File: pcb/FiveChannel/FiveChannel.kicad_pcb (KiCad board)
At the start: 2 copper layers, 47 x 31.4 mm, 22 parts, among them J101 UPDI, J102 5V In, J103 Conn_01x04_Male, J104 Conn_01x07_Male, J201 Conn_01x20_Male, U101 74LS595, U102 ATTINY1614

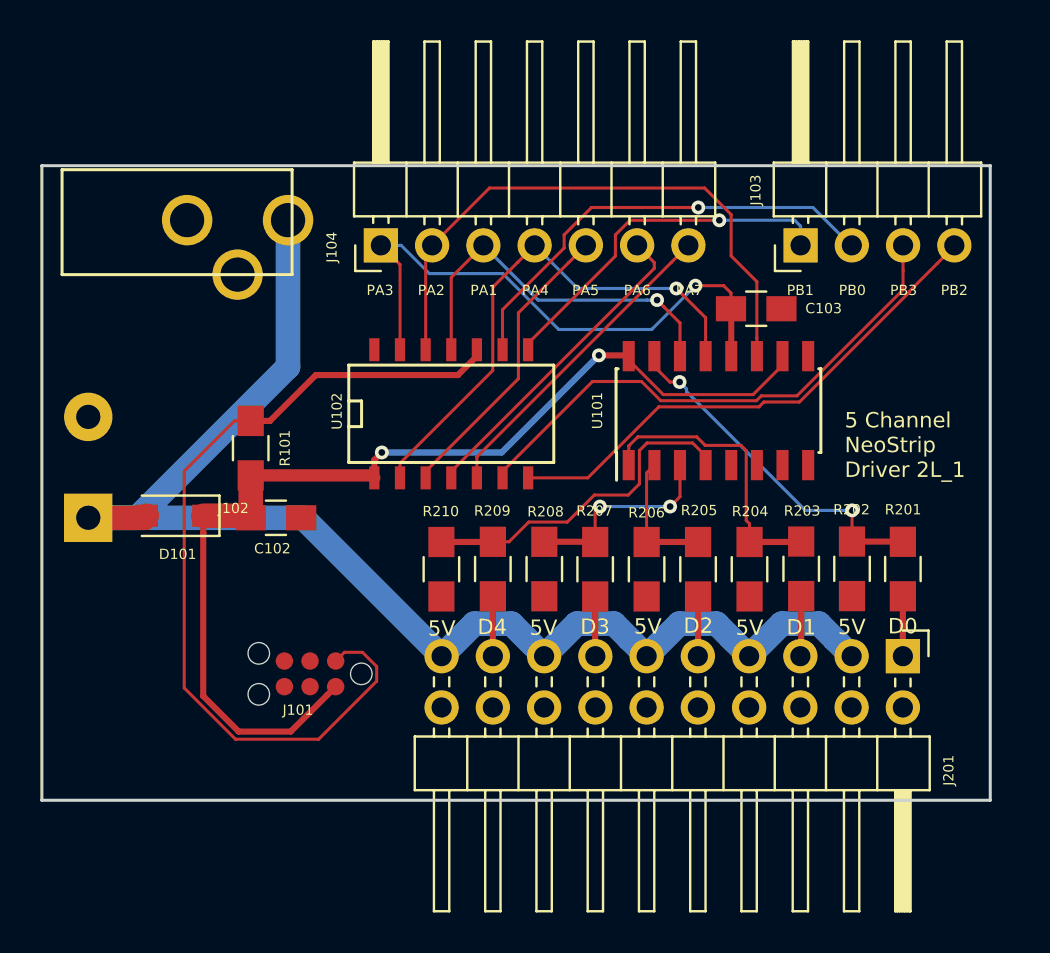
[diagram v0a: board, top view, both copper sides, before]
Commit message: Updates the schematic and PCB design to the lastest from the original repo
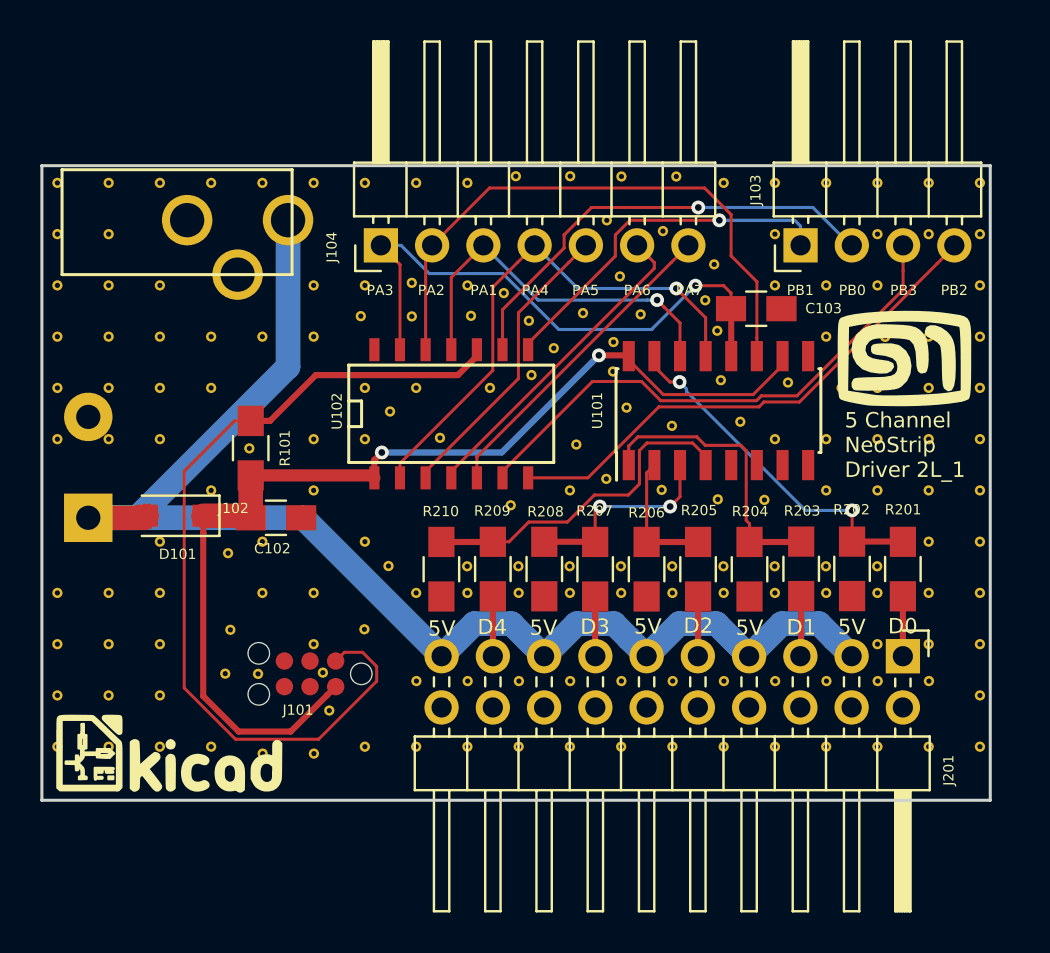
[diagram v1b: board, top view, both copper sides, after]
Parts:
- added G***: LOGO, advent_sternla:KiCad-Logo, F.Cu at (133.0, 78.5)
- added G***: LOGO, advent_sternla:MyBasic_rounded_50_1, F.Cu at (169.4, 58.9)
- added G***: LOGO, advent_sternla:MyBasic_rounded_50_1, B.Cu at (157.0, 64.3)
- added REF***: KiCad-Logo2_6mm_SilkScreen, Symbols:KiCad-Logo2_6mm_SilkScreen, B.Cu at (169.6, 64.2)
- added ST**: STITCH_VIA, advent_sternla:STITCH_VIA, F.Cu at (127.4, 50.3)
- added ST**: STITCH_VIA, advent_sternla:STITCH_VIA, F.Cu at (150.1, 49.9)
- added ST**: STITCH_VIA, advent_sternla:STITCH_VIA, F.Cu at (165.5, 65.5)
- added ST**: STITCH_VIA, advent_sternla:STITCH_VIA, F.Cu at (168.1, 65.5)
- added ST**: STITCH_VIA, advent_sternla:STITCH_VIA, F.Cu at (170.6, 65.5)
- added ST**: STITCH_VIA, advent_sternla:STITCH_VIA, F.Cu at (173.1, 65.5)
- added ST**: STITCH_VIA, advent_sternla:STITCH_VIA, F.Cu at (132.5, 68.0)
- added ST**: STITCH_VIA, advent_sternla:STITCH_VIA, F.Cu at (135.9, 68.6)
- added ST**: STITCH_VIA, advent_sternla:STITCH_VIA, F.Cu at (137.6, 68.0)
- added ST**: STITCH_VIA, advent_sternla:STITCH_VIA, F.Cu at (142.7, 68.0)
- added ST**: STITCH_VIA, advent_sternla:STITCH_VIA, F.Cu at (143.8, 69.2)
- added ST**: STITCH_VIA, advent_sternla:STITCH_VIA, F.Cu at (147.7, 69.3)
- added ST**: STITCH_VIA, advent_sternla:STITCH_VIA, F.Cu at (152.8, 49.9)
- added ST**: STITCH_VIA, advent_sternla:STITCH_VIA, F.Cu at (150.3, 69.3)
- added ST**: STITCH_VIA, advent_sternla:STITCH_VIA, F.Cu at (152.8, 69.3)
- added ST**: STITCH_VIA, advent_sternla:STITCH_VIA, F.Cu at (155.3, 69.3)
- added ST**: STITCH_VIA, advent_sternla:STITCH_VIA, F.Cu at (157.9, 69.3)
- added ST**: STITCH_VIA, advent_sternla:STITCH_VIA, F.Cu at (160.4, 69.3)
- added ST**: STITCH_VIA, advent_sternla:STITCH_VIA, F.Cu at (163.0, 69.3)
- added ST**: STITCH_VIA, advent_sternla:STITCH_VIA, F.Cu at (165.5, 69.3)
- added ST**: STITCH_VIA, advent_sternla:STITCH_VIA, F.Cu at (168.0, 69.3)
- added ST**: STITCH_VIA, advent_sternla:STITCH_VIA, F.Cu at (170.6, 68.0)
- added ST**: STITCH_VIA, advent_sternla:STITCH_VIA, F.Cu at (173.1, 68.0)
- added ST**: STITCH_VIA, advent_sternla:STITCH_VIA, F.Cu at (155.4, 49.9)
- added ST**: STITCH_VIA, advent_sternla:STITCH_VIA, F.Cu at (127.4, 70.6)
- added ST**: STITCH_VIA, advent_sternla:STITCH_VIA, F.Cu at (130.0, 70.6)
- added ST**: STITCH_VIA, advent_sternla:STITCH_VIA, F.Cu at (132.5, 70.6)
- added ST**: STITCH_VIA, advent_sternla:STITCH_VIA, F.Cu at (137.6, 70.6)
- added ST**: STITCH_VIA, advent_sternla:STITCH_VIA, F.Cu at (140.1, 70.6)
- added ST**: STITCH_VIA, advent_sternla:STITCH_VIA, F.Cu at (145.2, 70.6)
- added ST**: STITCH_VIA, advent_sternla:STITCH_VIA, F.Cu at (147.7, 70.6)
- added ST**: STITCH_VIA, advent_sternla:STITCH_VIA, F.Cu at (150.3, 70.6)
- added ST**: STITCH_VIA, advent_sternla:STITCH_VIA, F.Cu at (152.8, 70.6)
- added ST**: STITCH_VIA, advent_sternla:STITCH_VIA, F.Cu at (155.4, 70.6)
- added ST**: STITCH_VIA, advent_sternla:STITCH_VIA, F.Cu at (158.1, 49.9)
- added ST**: STITCH_VIA, advent_sternla:STITCH_VIA, F.Cu at (157.9, 70.6)
- added ST**: STITCH_VIA, advent_sternla:STITCH_VIA, F.Cu at (160.4, 70.6)
- added ST**: STITCH_VIA, advent_sternla:STITCH_VIA, F.Cu at (163.0, 70.6)
- added ST**: STITCH_VIA, advent_sternla:STITCH_VIA, F.Cu at (165.5, 70.6)
- added ST**: STITCH_VIA, advent_sternla:STITCH_VIA, F.Cu at (168.1, 70.6)
- added ST**: STITCH_VIA, advent_sternla:STITCH_VIA, F.Cu at (170.6, 70.6)
- added ST**: STITCH_VIA, advent_sternla:STITCH_VIA, F.Cu at (173.1, 70.6)
- added ST**: STITCH_VIA, advent_sternla:STITCH_VIA, F.Cu at (127.4, 73.1)
- added ST**: STITCH_VIA, advent_sternla:STITCH_VIA, F.Cu at (130.0, 73.1)
- added ST**: STITCH_VIA, advent_sternla:STITCH_VIA, F.Cu at (132.5, 73.1)
- added ST**: STITCH_VIA, advent_sternla:STITCH_VIA, F.Cu at (160.4, 50.3)
- added ST**: STITCH_VIA, advent_sternla:STITCH_VIA, F.Cu at (137.4, 74.6)
- added ST**: STITCH_VIA, advent_sternla:STITCH_VIA, F.Cu at (140.1, 73.1)
- added ST**: STITCH_VIA, advent_sternla:STITCH_VIA, F.Cu at (142.6, 72.4)
- added ST**: STITCH_VIA, advent_sternla:STITCH_VIA, F.Cu at (168.1, 73.1)
- added ST**: STITCH_VIA, advent_sternla:STITCH_VIA, F.Cu at (170.6, 73.1)
- added ST**: STITCH_VIA, advent_sternla:STITCH_VIA, F.Cu at (173.1, 73.1)
- added ST**: STITCH_VIA, advent_sternla:STITCH_VIA, F.Cu at (127.4, 75.7)
- added ST**: STITCH_VIA, advent_sternla:STITCH_VIA, F.Cu at (130.0, 75.7)
- added ST**: STITCH_VIA, advent_sternla:STITCH_VIA, F.Cu at (132.5, 75.7)
- added ST**: STITCH_VIA, advent_sternla:STITCH_VIA, F.Cu at (136.0, 72.4)
- added ST**: STITCH_VIA, advent_sternla:STITCH_VIA, F.Cu at (163.0, 50.3)
- added ST**: STITCH_VIA, advent_sternla:STITCH_VIA, F.Cu at (140.6, 74.5)
- added ST**: STITCH_VIA, advent_sternla:STITCH_VIA, F.Cu at (140.9, 76.4)
- added ST**: STITCH_VIA, advent_sternla:STITCH_VIA, F.Cu at (145.2, 74.9)
- added ST**: STITCH_VIA, advent_sternla:STITCH_VIA, F.Cu at (147.8, 74.9)
- added ST**: STITCH_VIA, advent_sternla:STITCH_VIA, F.Cu at (150.3, 74.9)
- added ST**: STITCH_VIA, advent_sternla:STITCH_VIA, F.Cu at (152.8, 74.9)
- added ST**: STITCH_VIA, advent_sternla:STITCH_VIA, F.Cu at (155.4, 74.9)
- added ST**: STITCH_VIA, advent_sternla:STITCH_VIA, F.Cu at (157.9, 74.9)
- added ST**: STITCH_VIA, advent_sternla:STITCH_VIA, F.Cu at (160.5, 74.9)
- added ST**: STITCH_VIA, advent_sternla:STITCH_VIA, F.Cu at (163.0, 74.9)
- added ST**: STITCH_VIA, advent_sternla:STITCH_VIA, F.Cu at (165.5, 50.3)
- added ST**: STITCH_VIA, advent_sternla:STITCH_VIA, F.Cu at (165.5, 74.9)
- added ST**: STITCH_VIA, advent_sternla:STITCH_VIA, F.Cu at (168.1, 74.9)
- added ST**: STITCH_VIA, advent_sternla:STITCH_VIA, F.Cu at (170.6, 74.9)
- added ST**: STITCH_VIA, advent_sternla:STITCH_VIA, F.Cu at (173.1, 75.7)
- added ST**: STITCH_VIA, advent_sternla:STITCH_VIA, F.Cu at (127.4, 78.2)
- added ST**: STITCH_VIA, advent_sternla:STITCH_VIA, F.Cu at (130.0, 78.2)
- added ST**: STITCH_VIA, advent_sternla:STITCH_VIA, F.Cu at (132.5, 78.2)
- added ST**: STITCH_VIA, advent_sternla:STITCH_VIA, F.Cu at (135.0, 78.2)
- added ST**: STITCH_VIA, advent_sternla:STITCH_VIA, F.Cu at (137.6, 78.5)
- added ST**: STITCH_VIA, advent_sternla:STITCH_VIA, F.Cu at (140.1, 78.5)
- added ST**: STITCH_VIA, advent_sternla:STITCH_VIA, F.Cu at (168.1, 50.3)
- added ST**: STITCH_VIA, advent_sternla:STITCH_VIA, F.Cu at (142.7, 78.2)
- added ST**: STITCH_VIA, advent_sternla:STITCH_VIA, F.Cu at (145.2, 78.2)
- added ST**: STITCH_VIA, advent_sternla:STITCH_VIA, F.Cu at (147.7, 78.2)
- added ST**: STITCH_VIA, advent_sternla:STITCH_VIA, F.Cu at (150.3, 78.2)
- added ST**: STITCH_VIA, advent_sternla:STITCH_VIA, F.Cu at (152.8, 78.2)
- added ST**: STITCH_VIA, advent_sternla:STITCH_VIA, F.Cu at (155.4, 78.2)
- added ST**: STITCH_VIA, advent_sternla:STITCH_VIA, F.Cu at (157.9, 78.2)
- added ST**: STITCH_VIA, advent_sternla:STITCH_VIA, F.Cu at (160.4, 78.2)
- added ST**: STITCH_VIA, advent_sternla:STITCH_VIA, F.Cu at (163.0, 78.2)
- added ST**: STITCH_VIA, advent_sternla:STITCH_VIA, F.Cu at (165.5, 78.2)
- added ST**: STITCH_VIA, advent_sternla:STITCH_VIA, F.Cu at (170.6, 50.3)
- added ST**: STITCH_VIA, advent_sternla:STITCH_VIA, F.Cu at (168.1, 78.2)
- added ST**: STITCH_VIA, advent_sternla:STITCH_VIA, F.Cu at (170.6, 78.2)
- added ST**: STITCH_VIA, advent_sternla:STITCH_VIA, F.Cu at (173.1, 78.2)
- added ST**: STITCH_VIA, advent_sternla:STITCH_VIA, F.Cu at (143.9, 61.6)
- added ST**: STITCH_VIA, advent_sternla:STITCH_VIA, F.Cu at (155.0, 59.6)
- added ST**: STITCH_VIA, advent_sternla:STITCH_VIA, F.Cu at (135.7, 74.6)
- added ST**: STITCH_VIA, advent_sternla:STITCH_VIA, F.Cu at (173.1, 50.3)
- added ST**: STITCH_VIA, advent_sternla:STITCH_VIA, F.Cu at (130.0, 50.3)
- added ST**: STITCH_VIA, advent_sternla:STITCH_VIA, F.Cu at (127.4, 52.8)
- added ST**: STITCH_VIA, advent_sternla:STITCH_VIA, F.Cu at (130.0, 52.8)
- added ST**: STITCH_VIA, advent_sternla:STITCH_VIA, F.Cu at (160.0, 54.3)
- added ST**: STITCH_VIA, advent_sternla:STITCH_VIA, F.Cu at (163.0, 52.8)
- added ST**: STITCH_VIA, advent_sternla:STITCH_VIA, F.Cu at (168.1, 52.8)
- added ST**: STITCH_VIA, advent_sternla:STITCH_VIA, F.Cu at (170.6, 52.8)
- added ST**: STITCH_VIA, advent_sternla:STITCH_VIA, F.Cu at (173.1, 52.8)
- added ST**: STITCH_VIA, advent_sternla:STITCH_VIA, F.Cu at (127.4, 55.3)
- added ST**: STITCH_VIA, advent_sternla:STITCH_VIA, F.Cu at (130.0, 55.3)
- added ST**: STITCH_VIA, advent_sternla:STITCH_VIA, F.Cu at (132.5, 55.3)
- added ST**: STITCH_VIA, advent_sternla:STITCH_VIA, F.Cu at (132.5, 50.3)
- added ST**: STITCH_VIA, advent_sternla:STITCH_VIA, F.Cu at (157.4, 52.6)
- added ST**: STITCH_VIA, advent_sternla:STITCH_VIA, F.Cu at (154.6, 52.1)
- added ST**: STITCH_VIA, advent_sternla:STITCH_VIA, F.Cu at (140.1, 55.3)
- added ST**: STITCH_VIA, advent_sternla:STITCH_VIA, F.Cu at (142.7, 55.3)
- added ST**: STITCH_VIA, advent_sternla:STITCH_VIA, F.Cu at (145.0, 55.2)
- added ST**: STITCH_VIA, advent_sternla:STITCH_VIA, F.Cu at (147.7, 55.3)
- added ST**: STITCH_VIA, advent_sternla:STITCH_VIA, F.Cu at (149.5, 55.7)
- added ST**: STITCH_VIA, advent_sternla:STITCH_VIA, F.Cu at (153.5, 56.7)
- added ST**: STITCH_VIA, advent_sternla:STITCH_VIA, F.Cu at (155.3, 54.9)
- added ST**: STITCH_VIA, advent_sternla:STITCH_VIA, F.Cu at (156.3, 56.8)
- added ST**: STITCH_VIA, advent_sternla:STITCH_VIA, F.Cu at (135.0, 50.3)
- added ST**: STITCH_VIA, advent_sternla:STITCH_VIA, F.Cu at (159.5, 56.1)
- added ST**: STITCH_VIA, advent_sternla:STITCH_VIA, F.Cu at (163.0, 55.3)
- added ST**: STITCH_VIA, advent_sternla:STITCH_VIA, F.Cu at (165.5, 55.3)
- added ST**: STITCH_VIA, advent_sternla:STITCH_VIA, F.Cu at (168.1, 55.3)
- added ST**: STITCH_VIA, advent_sternla:STITCH_VIA, F.Cu at (173.1, 55.3)
- added ST**: STITCH_VIA, advent_sternla:STITCH_VIA, F.Cu at (127.4, 57.9)
- added ST**: STITCH_VIA, advent_sternla:STITCH_VIA, F.Cu at (130.0, 57.9)
- added ST**: STITCH_VIA, advent_sternla:STITCH_VIA, F.Cu at (132.5, 57.9)
- added ST**: STITCH_VIA, advent_sternla:STITCH_VIA, F.Cu at (135.0, 57.9)
- added ST**: STITCH_VIA, advent_sternla:STITCH_VIA, F.Cu at (137.6, 57.9)
- added ST**: STITCH_VIA, advent_sternla:STITCH_VIA, F.Cu at (137.6, 50.3)
- added ST**: STITCH_VIA, advent_sternla:STITCH_VIA, F.Cu at (140.1, 57.9)
- added ST**: STITCH_VIA, advent_sternla:STITCH_VIA, F.Cu at (142.5, 56.9)
- added ST**: STITCH_VIA, advent_sternla:STITCH_VIA, F.Cu at (145.0, 56.9)
- added ST**: STITCH_VIA, advent_sternla:STITCH_VIA, F.Cu at (147.9, 56.8)
- added ST**: STITCH_VIA, advent_sternla:STITCH_VIA, F.Cu at (150.8, 57.1)
- added ST**: STITCH_VIA, advent_sternla:STITCH_VIA, F.Cu at (152.0, 58.4)
- added ST**: STITCH_VIA, advent_sternla:STITCH_VIA, F.Cu at (155.0, 58.1)
- added ST**: STITCH_VIA, advent_sternla:STITCH_VIA, F.Cu at (160.1, 57.6)
- added ST**: STITCH_VIA, advent_sternla:STITCH_VIA, F.Cu at (165.5, 57.9)
- added ST**: STITCH_VIA, advent_sternla:STITCH_VIA, F.Cu at (168.4, 57.9)
- added ST**: STITCH_VIA, advent_sternla:STITCH_VIA, F.Cu at (140.1, 50.3)
- added ST**: STITCH_VIA, advent_sternla:STITCH_VIA, F.Cu at (170.6, 57.9)
- added ST**: STITCH_VIA, advent_sternla:STITCH_VIA, F.Cu at (173.1, 57.9)
- added ST**: STITCH_VIA, advent_sternla:STITCH_VIA, F.Cu at (127.4, 60.4)
- added ST**: STITCH_VIA, advent_sternla:STITCH_VIA, F.Cu at (130.0, 60.4)
- added ST**: STITCH_VIA, advent_sternla:STITCH_VIA, F.Cu at (132.5, 60.4)
- added ST**: STITCH_VIA, advent_sternla:STITCH_VIA, F.Cu at (135.0, 60.4)
- added ST**: STITCH_VIA, advent_sternla:STITCH_VIA, F.Cu at (142.7, 60.4)
- added ST**: STITCH_VIA, advent_sternla:STITCH_VIA, F.Cu at (145.2, 60.4)
- added ST**: STITCH_VIA, advent_sternla:STITCH_VIA, F.Cu at (148.9, 60.4)
- added ST**: STITCH_VIA, advent_sternla:STITCH_VIA, F.Cu at (150.9, 59.8)
- added ST**: STITCH_VIA, advent_sternla:STITCH_VIA, F.Cu at (142.7, 50.3)
- added ST**: STITCH_VIA, advent_sternla:STITCH_VIA, F.Cu at (160.3, 60.0)
- added ST**: STITCH_VIA, advent_sternla:STITCH_VIA, F.Cu at (163.6, 60.1)
- added ST**: STITCH_VIA, advent_sternla:STITCH_VIA, F.Cu at (166.3, 60.4)
- added ST**: STITCH_VIA, advent_sternla:STITCH_VIA, F.Cu at (168.1, 60.4)
- added ST**: STITCH_VIA, advent_sternla:STITCH_VIA, F.Cu at (170.6, 60.4)
- added ST**: STITCH_VIA, advent_sternla:STITCH_VIA, F.Cu at (173.1, 60.4)
- added ST**: STITCH_VIA, advent_sternla:STITCH_VIA, F.Cu at (127.4, 63.0)
- added ST**: STITCH_VIA, advent_sternla:STITCH_VIA, F.Cu at (130.0, 63.0)
- added ST**: STITCH_VIA, advent_sternla:STITCH_VIA, F.Cu at (132.5, 63.0)
- added ST**: STITCH_VIA, advent_sternla:STITCH_VIA, F.Cu at (136.9, 63.4)
- added ST**: STITCH_VIA, advent_sternla:STITCH_VIA, F.Cu at (145.2, 50.3)
- added ST**: STITCH_VIA, advent_sternla:STITCH_VIA, F.Cu at (140.1, 63.0)
- added ST**: STITCH_VIA, advent_sternla:STITCH_VIA, F.Cu at (142.7, 63.0)
- added ST**: STITCH_VIA, advent_sternla:STITCH_VIA, F.Cu at (146.4, 62.9)
- added ST**: STITCH_VIA, advent_sternla:STITCH_VIA, F.Cu at (153.1, 63.2)
- added ST**: STITCH_VIA, advent_sternla:STITCH_VIA, F.Cu at (155.6, 61.4)
- added ST**: STITCH_VIA, advent_sternla:STITCH_VIA, F.Cu at (157.9, 62.3)
- added ST**: STITCH_VIA, advent_sternla:STITCH_VIA, F.Cu at (161.3, 62.1)
- added ST**: STITCH_VIA, advent_sternla:STITCH_VIA, F.Cu at (163.0, 63.0)
- added ST**: STITCH_VIA, advent_sternla:STITCH_VIA, F.Cu at (165.5, 63.0)
- added ST**: STITCH_VIA, advent_sternla:STITCH_VIA, F.Cu at (168.1, 63.0)
- added ST**: STITCH_VIA, advent_sternla:STITCH_VIA, F.Cu at (147.7, 50.3)
- added ST**: STITCH_VIA, advent_sternla:STITCH_VIA, F.Cu at (170.6, 63.0)
- added ST**: STITCH_VIA, advent_sternla:STITCH_VIA, F.Cu at (173.1, 63.0)
- added ST**: STITCH_VIA, advent_sternla:STITCH_VIA, F.Cu at (135.0, 65.5)
- added ST**: STITCH_VIA, advent_sternla:STITCH_VIA, F.Cu at (140.1, 65.5)
- added ST**: STITCH_VIA, advent_sternla:STITCH_VIA, F.Cu at (149.9, 66.2)
- added ST**: STITCH_VIA, advent_sternla:STITCH_VIA, F.Cu at (152.8, 65.5)
- added ST**: STITCH_VIA, advent_sternla:STITCH_VIA, F.Cu at (154.6, 64.9)
- added ST**: STITCH_VIA, advent_sternla:STITCH_VIA, F.Cu at (157.4, 65.5)
- added ST**: STITCH_VIA, advent_sternla:STITCH_VIA, F.Cu at (160.1, 65.9)
- added ST**: STITCH_VIA, advent_sternla:STITCH_VIA, F.Cu at (162.5, 66.0)
- U101: value 74LS595 -> 74LS596
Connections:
- J101 pad 3: unconnected-(J101-Pin_3-Pad3) -> (no net)
- J101 pad 4: unconnected-(J101-Pin_4-Pad4) -> (no net)
- J101 pad 5: unconnected-(J101-Pin_5-Pad5) -> (no net)
- J102 pad 3: unconnected-(J102-Pad3) -> (no net)
- U101 pad 5: unconnected-(U101-QF-Pad5) -> (no net)
- U101 pad 6: unconnected-(U101-QG-Pad6) -> (no net)
- U101 pad 7: unconnected-(U101-QH-Pad7) -> (no net)
- U101 pad 9: unconnected-(U101-~{QH}-Pad9) -> (no net)
